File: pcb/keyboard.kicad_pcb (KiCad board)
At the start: 2 copper layers, 217.2 x 96 mm, 52 parts, among them J1 TRRS, SW11 11, SW12 12, SW13 13, SW14 14, SW15 15, SW16 16, SW17 17, SW18 18, SW19 19, SW21 21, SW22 22, SW23 23, SW24 24, SW25 25, SW26 26, SW27 27, SW28 28, SW29 29, SW31 31, SW32 32, SW33 33, SW34 34, SW35 35, SW36 36, SW37 37, SW38 38, SW39 39, SW41 41, SW42 42, SW43 43, SW45 45, SW46 46, SW47 47, SW48 48, SW49 49, U1 EliteC

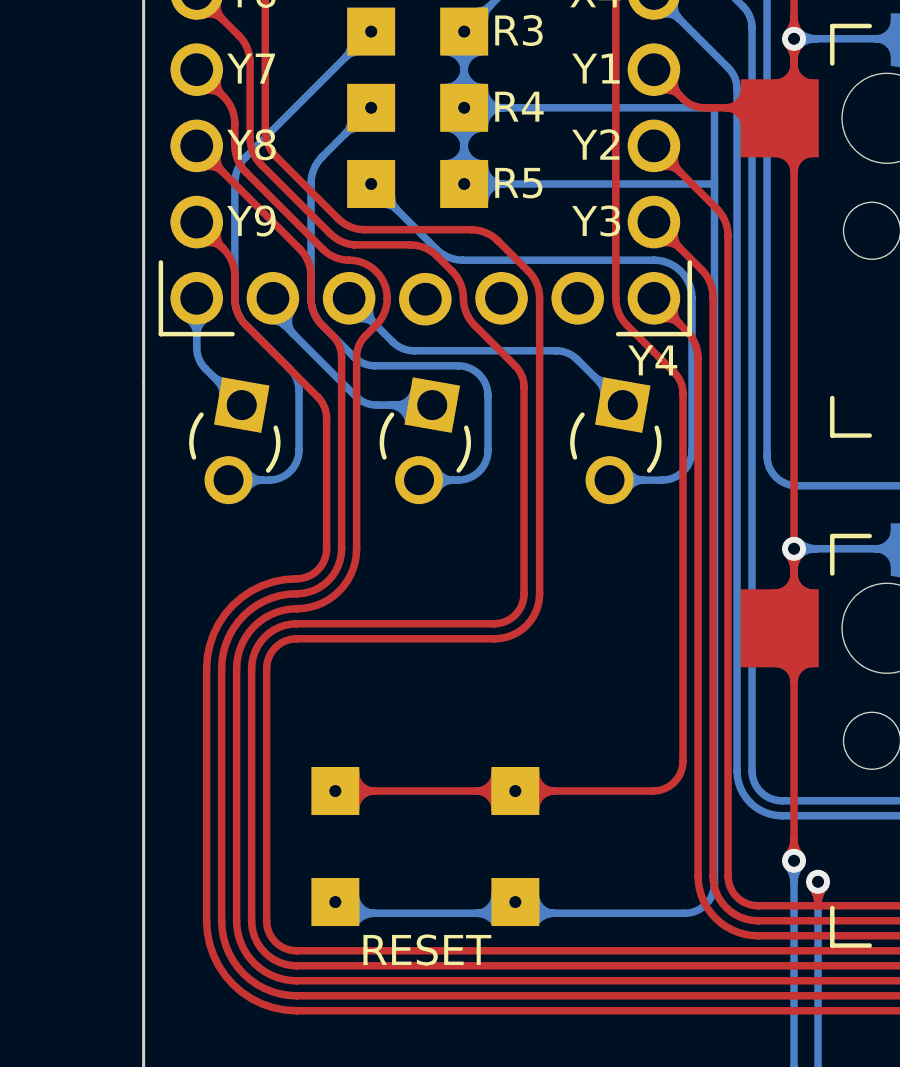
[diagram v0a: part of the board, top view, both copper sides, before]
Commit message: fix schematic of LED pins
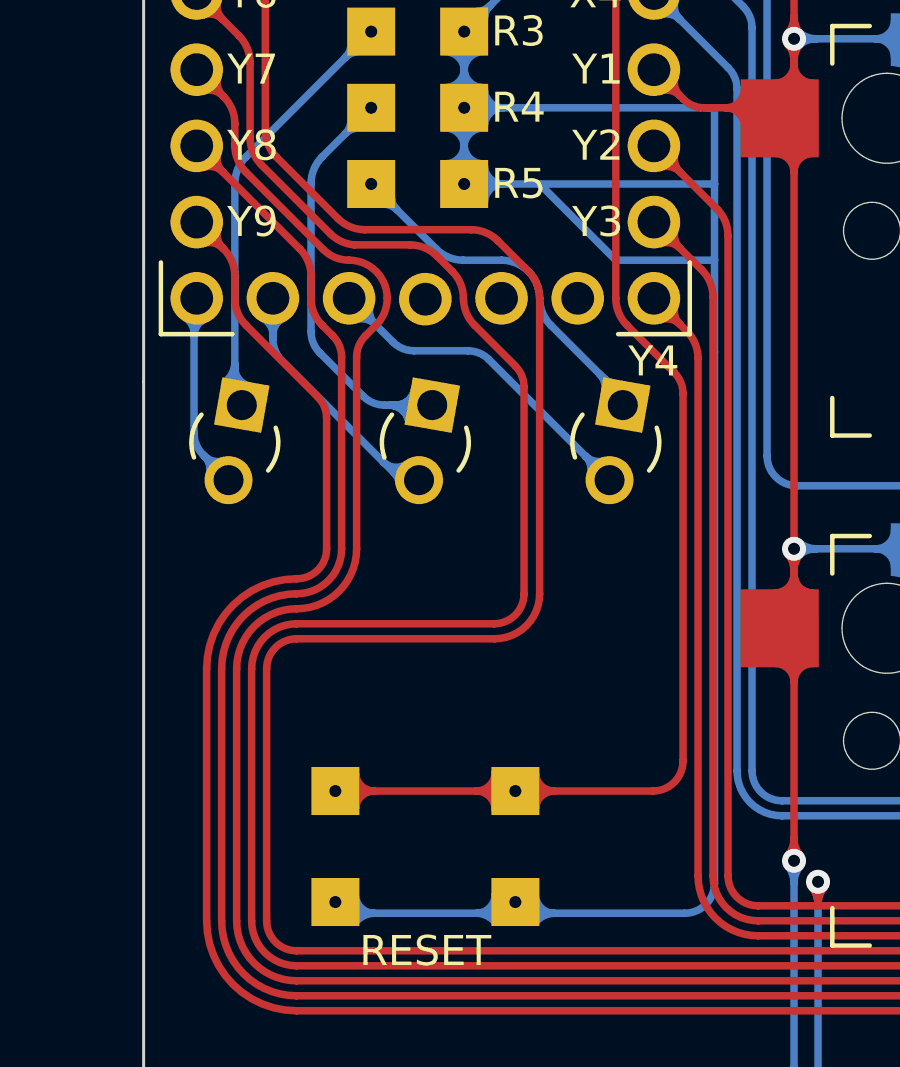
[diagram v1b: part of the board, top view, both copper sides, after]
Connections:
- D1 pad 1: LED1 -> Net-(D1-K)
- D1 pad 2: Net-(D1-A) -> LED1
- D2 pad 1: LED2 -> Net-(D2-K)
- D2 pad 2: Net-(D2-A) -> LED2
- D3 pad 1: LED3 -> Net-(D3-K)
- D3 pad 2: Net-(D3-A) -> LED3
- R3 pad 1: Net-(D1-A) -> Net-(D1-K)
- R4 pad 1: Net-(D2-A) -> Net-(D2-K)
- R5 pad 1: Net-(D3-A) -> Net-(D3-K)
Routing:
- net Net-(D3-A): track 22.9 -> 0.00 mm
- net Net-(D1-A): track 21.7 -> 0.00 mm
- net Net-(D2-A): track 21.6 -> 0.00 mm
- net Net-(D2-K): track 0.00 -> 17.9 mm
- net Net-(D1-K): track 0.00 -> 16.9 mm
- net Net-(D3-K): track 0.00 -> 13.9 mm
- net GND: track 150.6 -> 157.4 mm
- net LED1: track 6.62 -> 9.24 mm
- net LED2: track 10.1 -> 11.0 mm
- net LED3: track 12.9 -> 13.8 mm

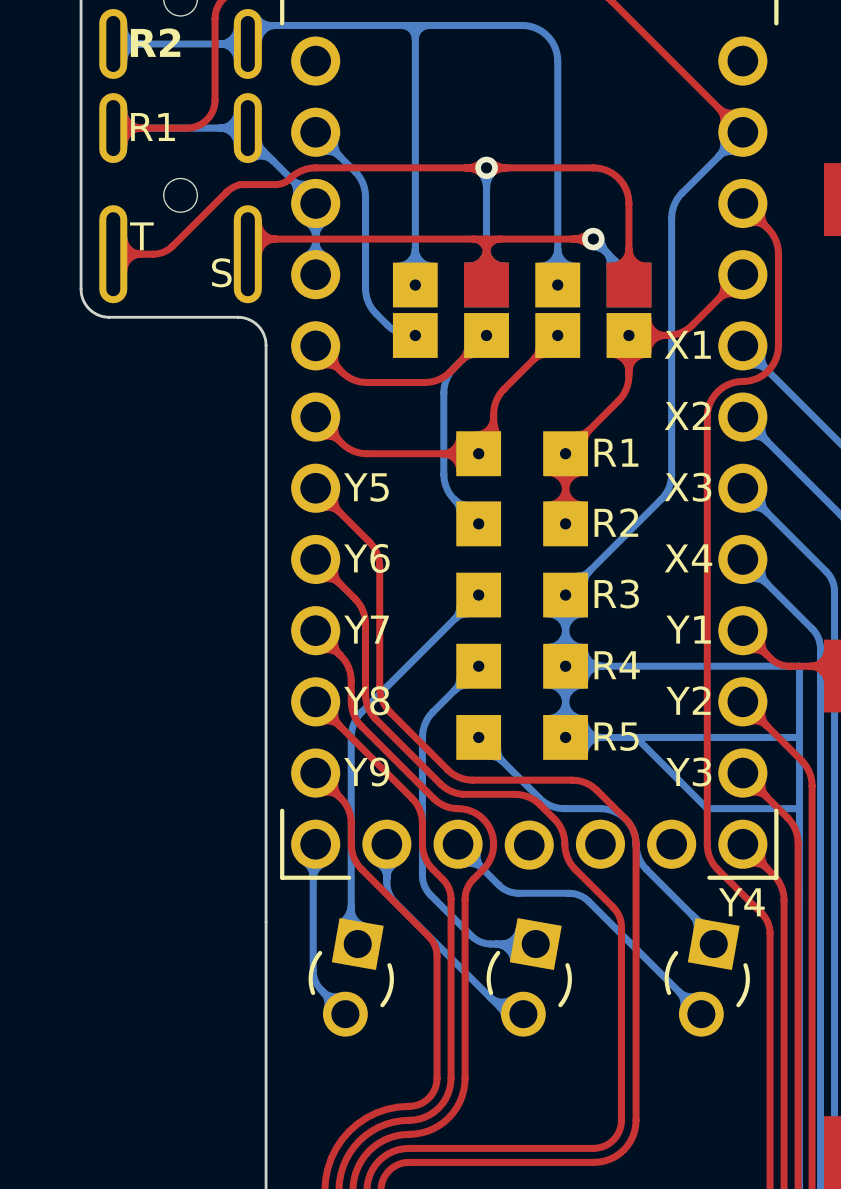
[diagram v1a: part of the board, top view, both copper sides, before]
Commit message: improve traces around microcontroller
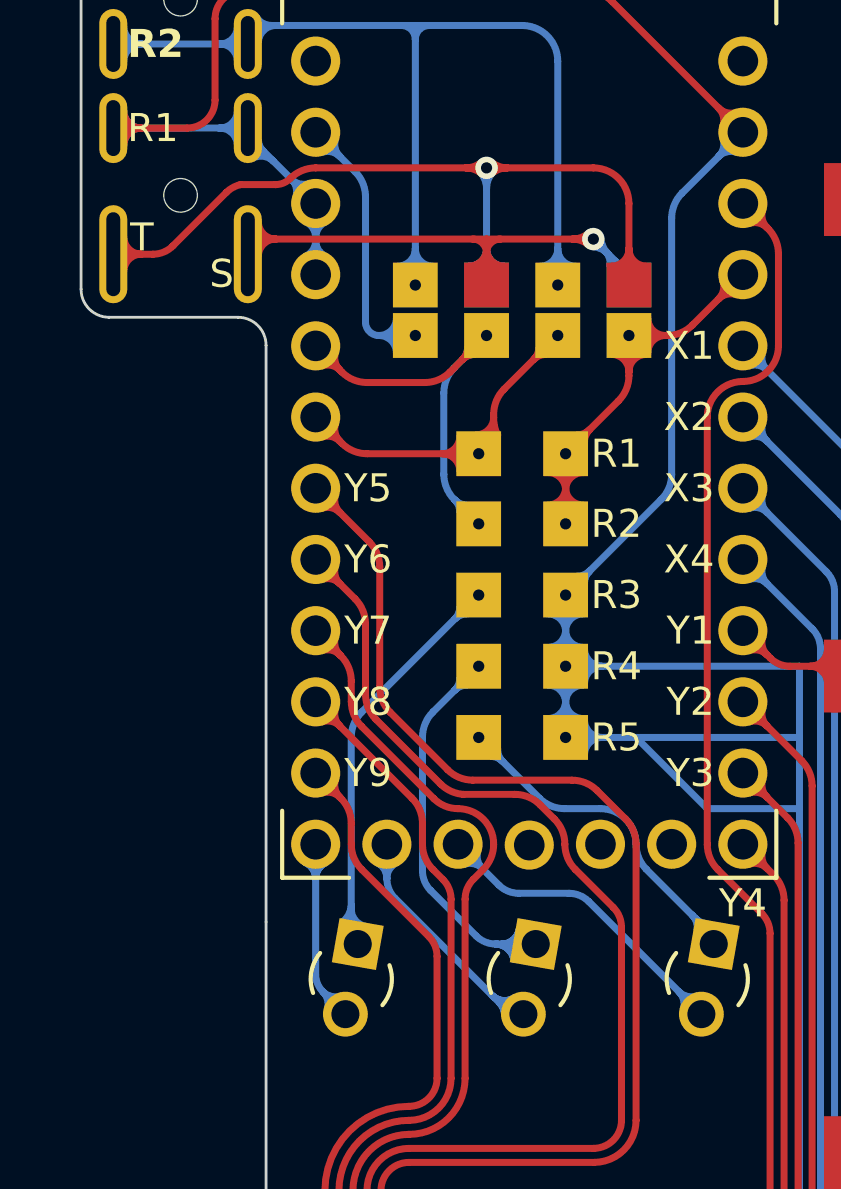
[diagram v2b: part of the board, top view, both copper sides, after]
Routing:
- net DATA: track 10.3 -> 12.7 mm
- net LED1: track 9.24 -> 10.7 mm

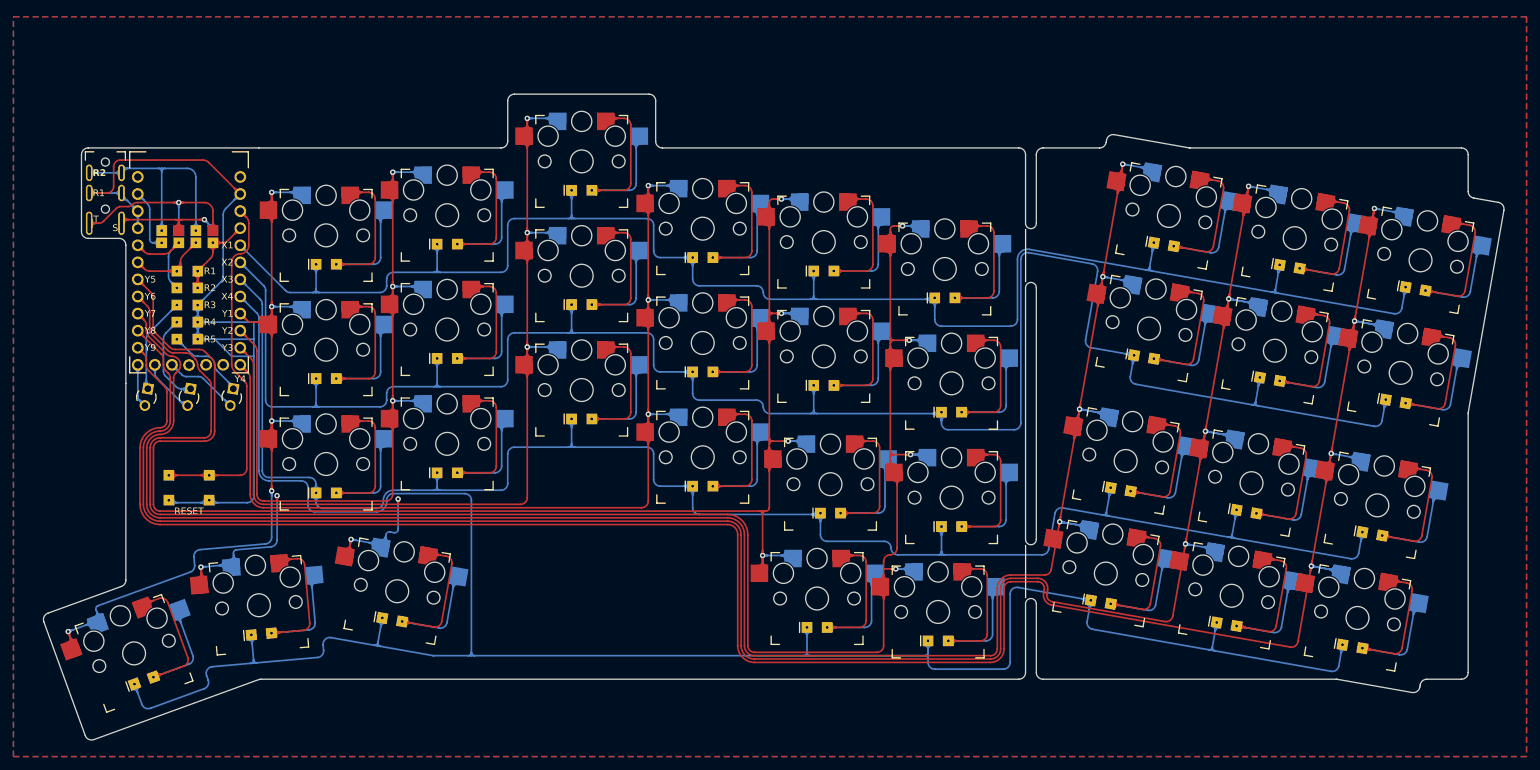
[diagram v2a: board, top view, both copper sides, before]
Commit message: start working on pinky separation; update layout and move some footprints
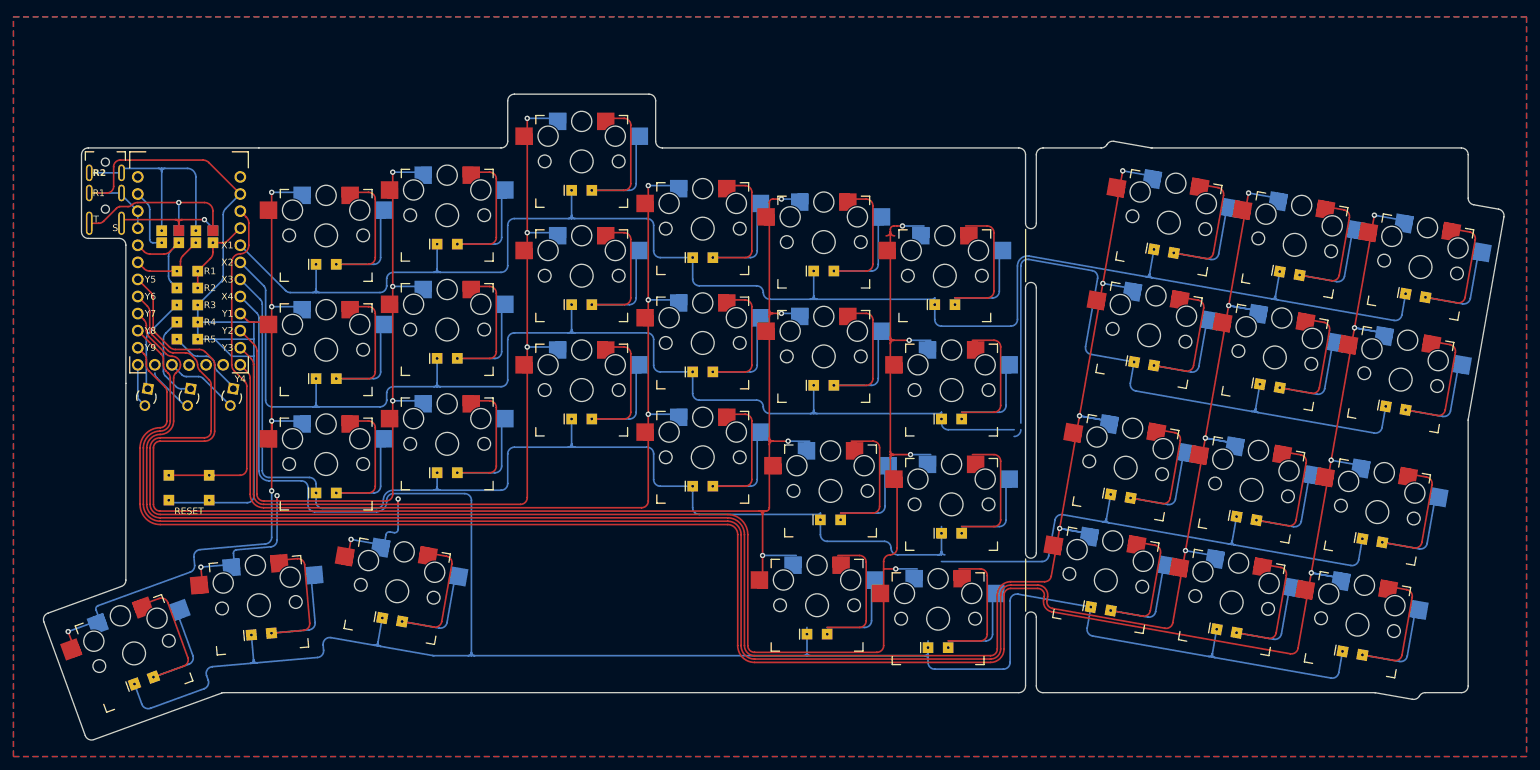
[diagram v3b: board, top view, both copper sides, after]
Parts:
- moved SW16 1.00 mm to (173.5, 68.5)
- moved SW17 1.00 mm to (206.8, 60.6)
- moved SW18 1.00 mm to (225.5, 63.9)
- moved SW19 1.00 mm to (244.2, 67.2)
- moved SW26 1.00 mm to (174.5, 85.5)
- moved SW27 1.00 mm to (203.9, 77.4)
- moved SW28 1.00 mm to (222.6, 80.7)
- moved SW29 1.00 mm to (241.3, 84.0)
- moved SW35 1.00 mm to (156.5, 100.5)
- moved SW36 1.00 mm to (174.5, 102.5)
- moved SW37 1.00 mm to (200.4, 97.0)
- moved SW38 1.00 mm to (219.1, 100.3)
- moved SW39 1.00 mm to (237.8, 103.6)
- moved SW45 1.00 mm to (154.5, 117.5)
- moved SW46 1.00 mm to (172.5, 119.5)
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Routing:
- net COL1: track 157.2 -> 115.2 mm
- net COL8: track 351.0 -> 310.4 mm
- net COL9: track 368.4 -> 327.8 mm
- net COL7: track 329.7 -> 289.1 mm
- net COL2: track 173.3 -> 133.9 mm
- net COL3: track 192.5 -> 153.2 mm
- net COL6: track 302.1 -> 267.7 mm
- net COL5: track 256.6 -> 222.8 mm
- net GND: track 157.4 -> 126.2 mm
- net COL4: track 171.2 -> 142.5 mm
- net ROW2: track 310.1 -> 284.9 mm
- net ROW3: track 278.1 -> 254.0 mm
- net ROW1: track 269.5 -> 246.2 mm
- net ROW4: track 343.6 -> 324.0 mm
- net VCC: track 22.5 -> 12.5 mm
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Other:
- outline, holes or cut-outs redrawn

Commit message: improve switch double pads
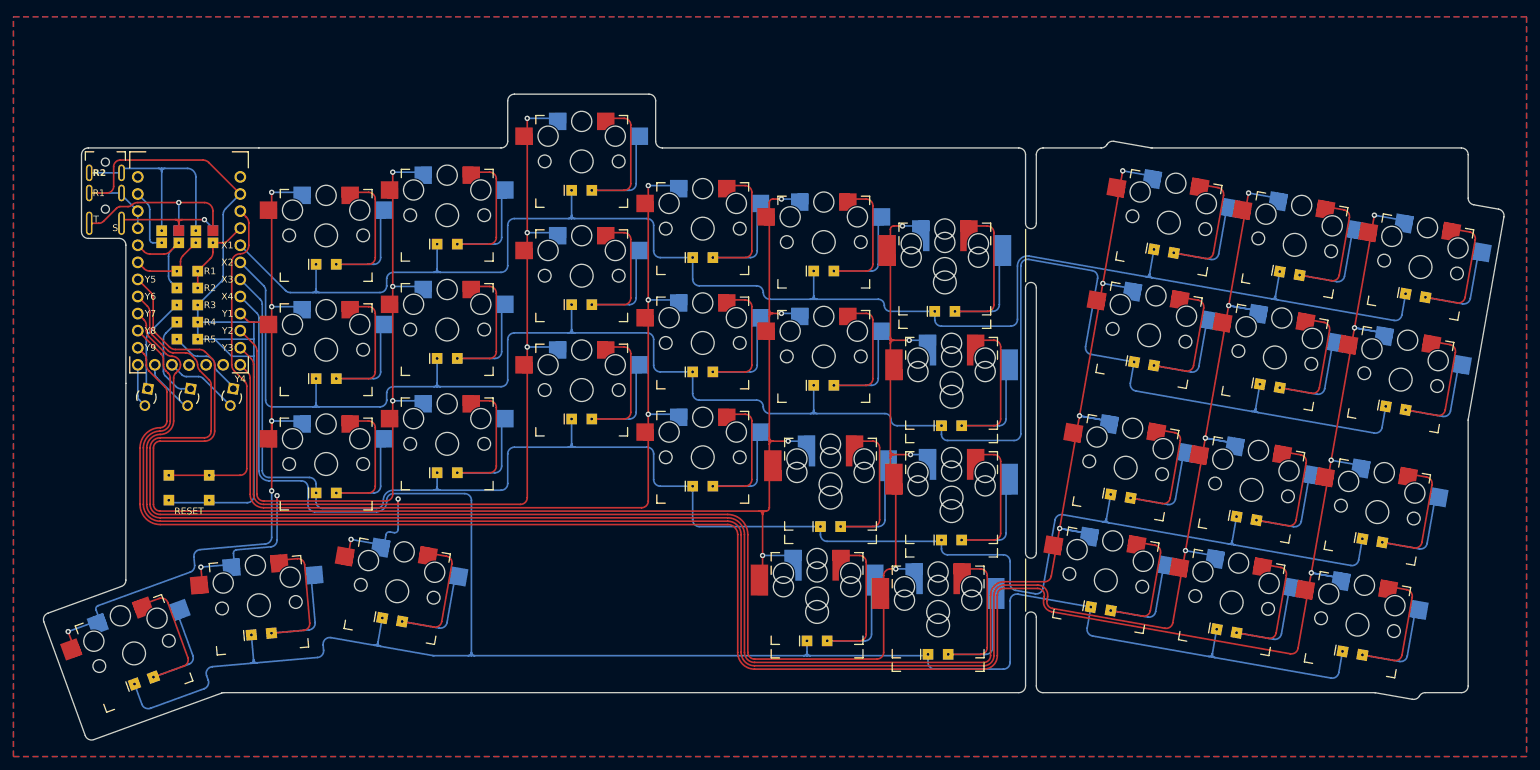
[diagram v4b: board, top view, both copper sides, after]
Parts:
- SW16, SW26, SW35, SW36, SW45, SW46: footprint Keyboard:Switch -> Keyboard:SwitchDouble
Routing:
- net ROW4: track 324.0 -> 318.6 mm
- net COL6: track 267.7 -> 263.9 mm
- net ROW3: track 254.0 -> 257.2 mm
- net ROW2: track 284.9 -> 287.1 mm
- net COL7: track 289.1 -> 291.1 mm
- net Net-(SW46-Pad3): track 33.5 -> 35.5 mm
- net Net-(SW45-Pad3): track 33.5 -> 35.5 mm
- net Net-(SW36-Pad3): track 33.5 -> 35.5 mm
- net Net-(SW35-Pad3): track 33.5 -> 35.5 mm
- net Net-(SW26-Pad3): track 33.5 -> 35.5 mm
- net Net-(SW16-Pad3): track 33.5 -> 35.5 mm
- net COL9: track 327.8 -> 329.8 mm
- net COL8: track 310.4 -> 312.4 mm
- net COL5: track 222.8 -> 224.8 mm
- net LED2: track 7.07 -> 8.29 mm
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
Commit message: move pinky up by 1mm
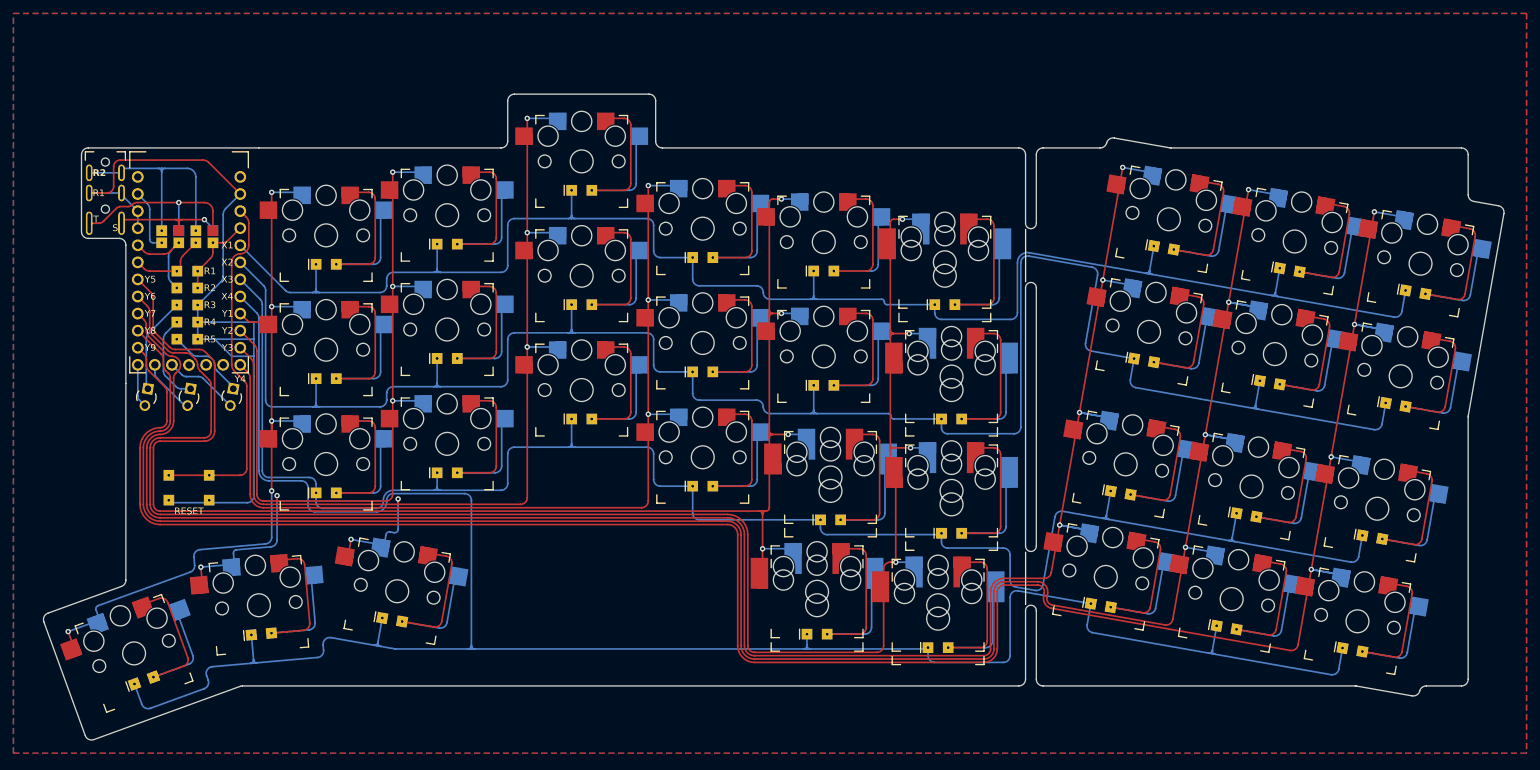
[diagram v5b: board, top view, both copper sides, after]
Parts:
- moved SW16 1.00 mm to (173.5, 67.5)
- moved SW26 1.00 mm to (174.5, 84.5)
- moved SW35 1.00 mm to (156.5, 99.5)
- moved SW36 1.00 mm to (174.5, 101.5)
- moved SW45 1.00 mm to (154.5, 116.5)
- moved SW46 1.00 mm to (172.5, 118.5)
- moved SW17 0.50 mm to (206.8, 60.1)
- moved SW18 0.50 mm to (225.5, 63.4)
- moved SW19 0.50 mm to (244.2, 66.7)
- moved SW27 0.50 mm to (203.9, 76.9)
- moved SW28 0.50 mm to (222.6, 80.2)
- moved SW29 0.50 mm to (241.3, 83.5)
- moved SW37 0.50 mm to (200.4, 96.5)
- moved SW38 0.50 mm to (219.1, 99.8)
- moved SW39 0.50 mm to (237.8, 103.1)
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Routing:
- net ROW4: track 318.6 -> 317.0 mm
- net COL8: track 312.4 -> 310.9 mm
- net COL9: track 329.8 -> 328.3 mm
- net COL7: track 291.1 -> 289.6 mm
- net ROW1: track 245.1 -> 244.1 mm
- net ROW2: track 287.1 -> 286.0 mm
- net COL5: track 224.8 -> 223.8 mm
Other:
- outline, holes or cut-outs redrawn
